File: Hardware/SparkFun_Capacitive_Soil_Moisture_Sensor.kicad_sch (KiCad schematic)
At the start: 32 parts, among them J1 Qwiic_RA, J2 Qwiic_RA, U1 CY8CMBR3102

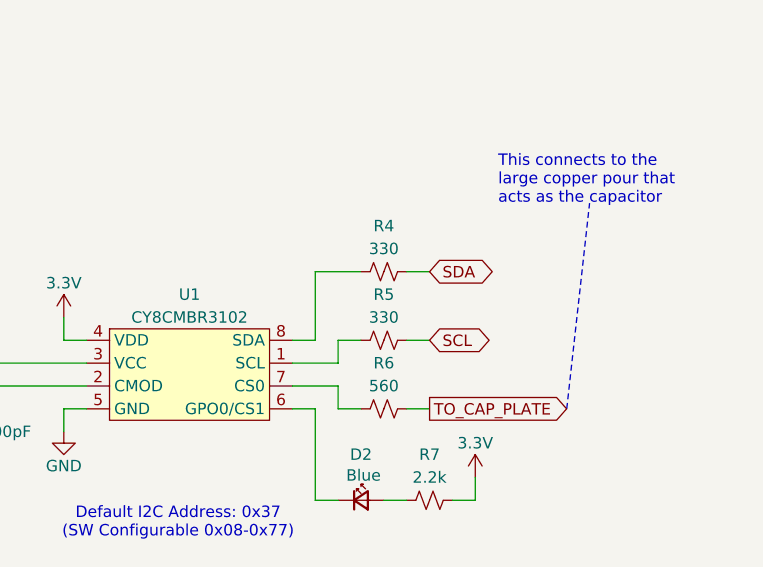
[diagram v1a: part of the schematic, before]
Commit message: Remove the 330 ohm series I2C resistors.
These resistors cause issues when you daisy chain qwiic devices as they
form a voltage divider with the pull-up resistance.
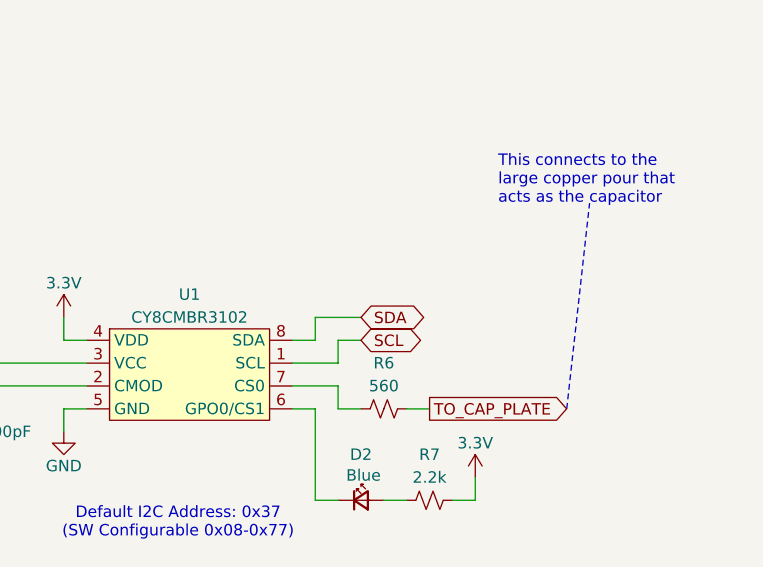
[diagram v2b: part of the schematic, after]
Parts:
- removed R4, R5: 330, SparkFun-Resistor:R_0603_1608Metric, symbol SparkFun-Resistor:330_0603
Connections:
- net SCL: now also U1.1 (SCL)
- net SDA: now also U1.8 (SDA)
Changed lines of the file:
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@@
 	(wire
 		(pts
-			(xy 231.14 76.2) (xy 233.68 76.2)
-		)
-		(stroke
-			(width 0)
-			(type default)
-		)
-	)
-	(wire
-		(pts
 			(xy 220.98 119.38) (xy 220.98 121.92)
 		)
@@
 	(wire
 		(pts
-			(xy 220.98 76.2) (xy 220.98 68.58)
+			(xy 220.98 76.2) (xy 220.98 73.66)
 		)
 		(stroke
@@
 	(wire
 		(pts
-			(xy 231.14 68.58) (xy 233.68 68.58)
-		)
-		(stroke
-			(width 0)
-			(type default)
-		)
-	)
-	(wire
-		(pts
 			(xy 193.04 83.82) (xy 193.04 86.36)
 		)
@@
 	(wire
 		(pts
-			(xy 220.98 68.58) (xy 226.06 68.58)
+			(xy 220.98 73.66) (xy 226.06 73.66)
 		)
 		(stroke
@@
 	(global_label "SDA"
 		(shape bidirectional)
-		(at 233.68 68.58 0)
+		(at 226.06 73.66 0)
 		(fields_autoplaced yes)
 		(effects
@@
 		)
 		(property "Intersheetrefs" "${INTERSHEET_REFS}"
-			(at 240.2333 68.58 0)
+			(at 232.6133 73.66 0)
 			(effects
 				(font
@@
 	(global_label "SCL"
 		(shape bidirectional)
-		(at 233.68 76.2 0)
+		(at 226.06 76.2 0)
 		(fields_autoplaced yes)
 		(effects
@@
 		)
 		(property "Intersheetrefs" "${INTERSHEET_REFS}"
-			(at 241.2841 76.2 0)
+			(at 233.6641 76.2 0)
 			(effects
 				(font
@@
 	)
 	(symbol
-		(lib_id "SparkFun-Resistor:330_0603")
-		(at 228.6 76.2 0)
-		(unit 1)
-		(exclude_from_sim no)
-		(in_bom yes)
-		(on_board yes)
-		(dnp no)
-		(property "Reference" "R5"
-			(at 228.6 71.12 0)
-			(effects
-				(font
-					(size 1.27 1.27)
-				)
-			)
-		)
-		(property "Value" "330"
-			(at 228.6 73.66 0)
-			(effects
-				(font
-					(size 1.27 1.27)
-				)
-			)
-		)
-		(property "Footprint" "SparkFun-Resistor:R_0603_1608Metric"
-			(at 228.6 80.772 0)
-			(effects
-				(font
-					(size 1.27 1.27)
-				)
-				(hide yes)
-			)
-		)
-		(property "Datasheet" "https://www.vishay.com/docs/20035/dcrcwe3.pdf"
-			(at 228.6 85.09 0)
-			(effects
-				(font
-					(size 1.27 1.27)
-				)
-				(hide yes)
-			)
-		)
-		(property "Description" "Resistor"
-			(at 228.6 87.63 0)
-			(effects
-				(font
-					(size 1.27 1.27)
-				)
-				(hide yes)
-			)
-		)
-		(property "PROD_ID" "RES-00818"
-			(at 228.6 83.058 0)
-			(effects
-				(font
-					(size 1.27 1.27)
-				)
-				(hide yes)
-			)
-		)
-		(pin "1"
-		)
-		(pin "2"
-		)
-		(instances
-			(project "SparkFun_Capacitive_Soil_Moisture_Sensor"
-				(path "/e3dd3ae4-244d-4cba-9cca-5d2abf83f29a"
-					(reference "R5")
-					(unit 1)
-				)
-			)
-		)
-	)
-	(symbol
 		(lib_id "SparkFun-LED:LED_Red_0603")
 		(at 86.36 167.64 90)
@@
 					(unit 1)
 				)
-			)
-		)
-	)
-	(symbol
-		(lib_id "SparkFun-Resistor:330_0603")
-		(at 228.6 68.58 0)
-		(unit 1)
-		(exclude_from_sim no)
-		(in_bom yes)
-		(on_board yes)
-		(dnp no)
-		(property "Reference" "R4"
-			(at 228.6 63.5 0)
-			(effects
-				(font
-					(size 1.27 1.27)
-				)
-			)
-		)
-		(property "Value" "330"
-			(at 228.6 66.04 0)
-			(effects
-				(font
-					(size 1.27 1.27)
-				)
-			)
-		)
-		(property "Footprint" "SparkFun-Resistor:R_0603_1608Metric"
-			(at 228.6 73.152 0)
-			(effects
-				(font
-					(size 1.27 1.27)
-				)
-				(hide yes)
-			)
-		)
-		(property "Datasheet" "https://www.vishay.com/docs/20035/dcrcwe3.pdf"
-			(at 228.6 77.47 0)
-			(effects
-				(font
-					(size 1.27 1.27)
-				)
-				(hide yes)
-			)
-		)
-		(property "Description" "Resistor"
-			(at 228.6 80.01 0)
-			(effects
-				(font
-					(size 1.27 1.27)
-				)
-				(hide yes)
-			)
-		)
-		(property "PROD_ID" "RES-00818"
-			(at 228.6 75.438 0)
-			(effects
-				(font
-					(size 1.27 1.27)
-				)
-				(hide yes)
-			)
-		)
-		(pin "1"
-		)
-		(pin "2"
-		)
-		(instances
-			(project ""
-				(path "/e3dd3ae4-244d-4cba-9cca-5d2abf83f29a"
-					(reference "R4")
-					(unit 1)
-				)

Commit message: Add changes from final review
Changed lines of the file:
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@@
 	(title_block
 		(title "SparkFun Capacitive Soil Moisture Sensor (Qwiic)")
-		(date "2025-12-02")
+		(date "2026-02-04")
 		(rev "v10")
 		(company "SparkFun Electronics")
@@
 		(on_board yes)
 		(dnp no)
-		(fields_autoplaced yes)
 		(property "Reference" "JP2"
 			(at 53.34 67.31 0)
@@
 					(size 1.27 1.27)
 				)
+				(hide yes)
 			)
 		)
 		(property "Value" "I2C"
-			(at 53.34 69.85 0)
+			(at 53.34 66.04 0)
 			(effects
 				(font
